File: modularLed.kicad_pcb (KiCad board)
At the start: 2 copper layers, 101.6 x 101.6 mm, 173 parts, among them IC101 ATMEGA328P-A, J101 POWER_JACKPTH, M301 FDS4935BZ, M302 FDS4935BZ, M303 FDS4935BZ, M304 FDS4935BZ, M305 FDS4935BZ, M306 FDS4935BZ, M307 FDS4935BZ, M308 FDS4935BZ, M401 FDS4935BZ, M402 FDS4935BZ, M403 FDS4935BZ, M404 FDS4935BZ, M405 FDS4935BZ, M406 FDS4935BZ, M407 FDS4935BZ, M408 FDS4935BZ, M501 FDS4935BZ, M502 FDS4935BZ, M503 FDS4935BZ, M504 FDS4935BZ, M505 FDS4935BZ, M506 FDS4935BZ, M507 FDS4935BZ, M508 FDS4935BZ, M601 FDS4935BZ, M602 FDS4935BZ, M603 FDS4935BZ, M604 FDS4935BZ, M605 FDS4935BZ, M606 FDS4935BZ, M607 FDS4935BZ, M608 FDS4935BZ, P101 CONN_01X04, P102 CONN_01X04, P103 CONN_01X04, P104 CONN_01X04, P105 CONN_01X06, P106 CONN_01X06, P107 CONN_01X06, P108 CONN_01X06, P109 CONN_02X03, P701 CONN_01X06, U101 ISL83485, U102 R-78E-0.5, U103 TLC5941, U104 74LS283, U105 74LS283, U201 74LS139, U301 74154, U401 74154, U501 74154, U601 74154, U701 ESP-12, U702 ISL83485

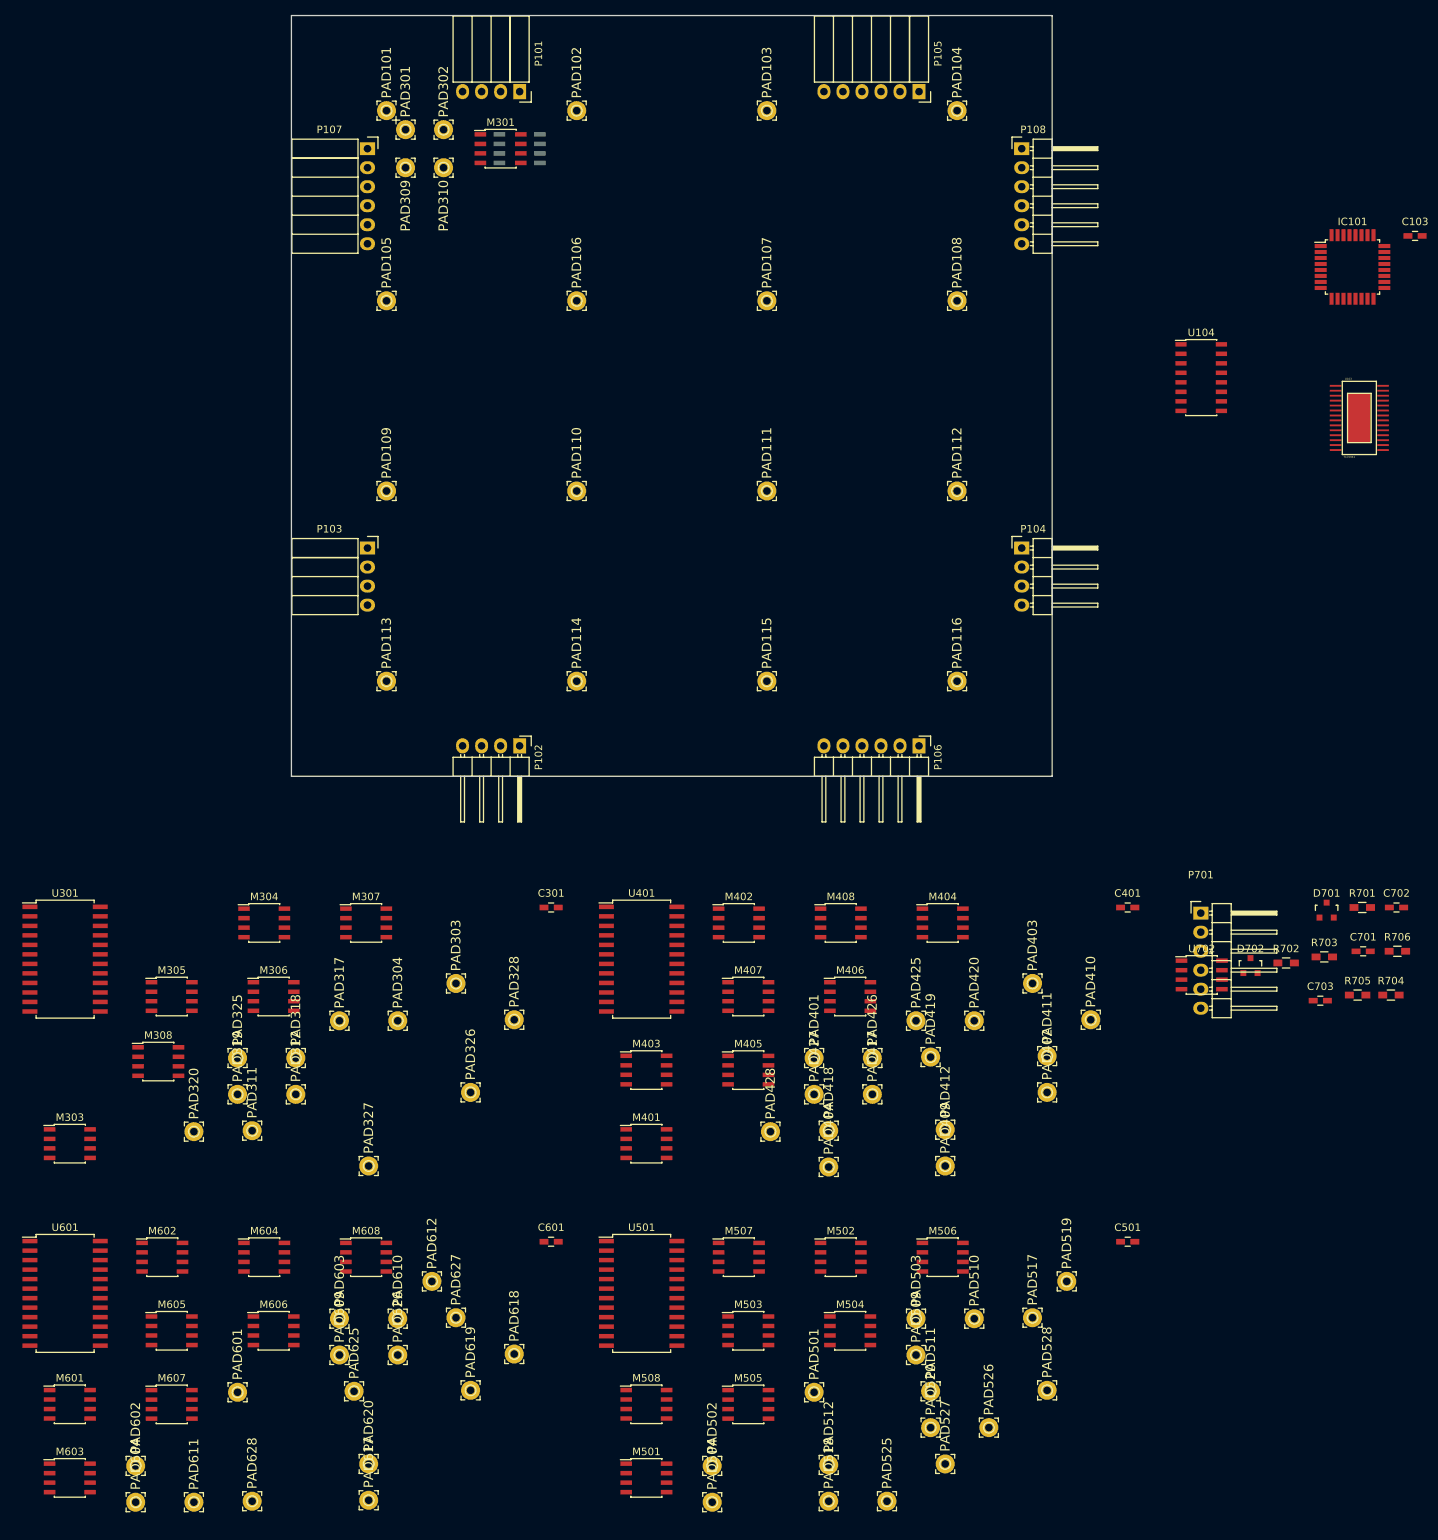
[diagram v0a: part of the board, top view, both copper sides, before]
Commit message: First quadrant of rows
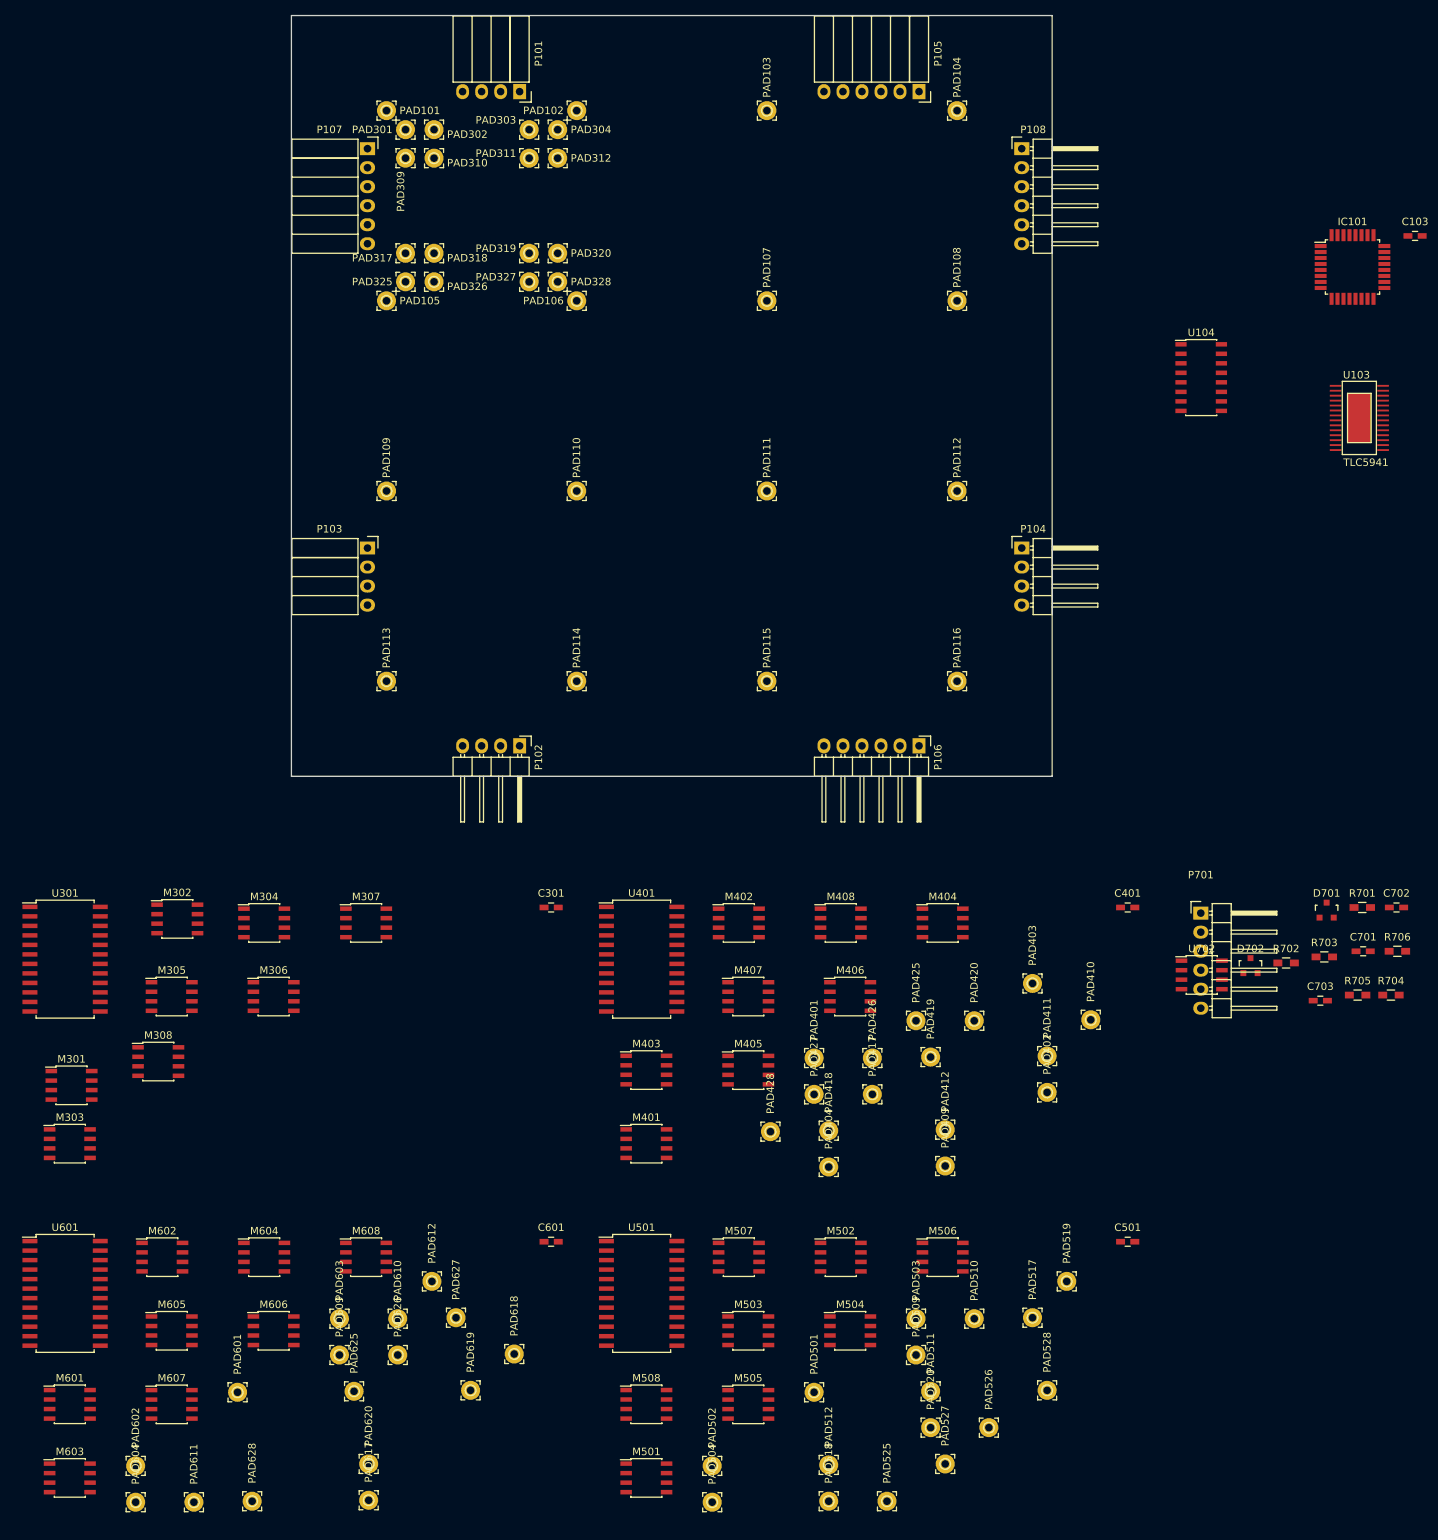
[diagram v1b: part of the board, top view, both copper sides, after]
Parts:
- M302: moved to F.Cu
- moved M301 137.6 mm to (59.5, 193.7)
- moved PAD311 135.0 mm to (120.7, 69.8), turned to 90 degrees
- moved PAD312 129.8 mm to (124.5, 69.8), turned to 270 degrees
- moved PAD320 127.0 mm to (124.5, 82.5), turned to 270 degrees
- moved PAD304 120.9 mm to (124.5, 66.0), turned to 270 degrees
- moved PAD327 120.0 mm to (120.7, 86.4), turned to 90 degrees
- moved PAD319 118.9 mm to (120.7, 82.5), turned to 90 degrees
- moved PAD303 114.4 mm to (120.7, 66.0), turned to 180 degrees
- moved M302 112.6 mm to (73.7, 171.4)
- moved PAD318 109.1 mm to (108.0, 82.5), turned to 270 degrees
- moved PAD326 108.4 mm to (108.0, 86.4), turned to 270 degrees
- moved PAD325 106.1 mm to (104.1, 86.4), turned to 90 degrees
- moved PAD317 102.9 mm to (104.1, 82.5), turned to 90 degrees
- moved PAD328 98.7 mm to (124.5, 86.4), turned to 270 degrees
- moved PAD310 1.80 mm to (108.0, 69.8), turned to 270 degrees
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
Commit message: Second quadrant of rows
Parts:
- moved PAD604 212.3 mm to (175.3, 66.0)
- moved PAD611 203.4 mm to (171.4, 69.8)
- moved PAD602 200.2 mm to (158.8, 66.0)
- moved PAD628 186.9 mm to (175.3, 86.4)
- moved PAD601 183.8 mm to (154.9, 66.0)
- moved PAD620 178.7 mm to (175.3, 82.5)
- moved PAD603 176.1 mm to (171.4, 66.0)
- moved PAD617 175.6 mm to (154.9, 82.5)
- moved PAD609 170.6 mm to (154.9, 69.8)
- moved PAD610 164.7 mm to (158.8, 69.8)
- moved PAD612 164.5 mm to (175.3, 69.8)
- moved PAD619 162.8 mm to (171.4, 82.5)
- moved PAD625 159.0 mm to (154.9, 86.4)
- moved PAD626 153.8 mm to (158.8, 86.4)
- moved PAD618 152.4 mm to (158.8, 82.5)
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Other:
- board text added: "Rows 0-15"
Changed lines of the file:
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@@
     (links 478)
     (no_connects 478)
-    (area 88.824999 50.724999 190.575001 152.475001)
+    (area 28.736999 47.3025 279.520234 278.695311)
     (thickness 1.6)
-    (drawings 4)
+    (drawings 5)
     (tracks 0)
     (zones 0)
@@
   )
   (module Wire_Pads:wirepad-2_54_1_0 (layer F.Cu)
-    (at 81.707143 234.670461)
+    (at 154.94 66.04)
     (descr "THROUGH-HOLE PAD")
     (tags "THROUGH-HOLE PAD")
@@
   )
   (module Wire_Pads:wirepad-2_54_1_0 (layer F.Cu)
-    (at 68.097143 244.500461)
+    (at 158.75 66.04)
     (descr "THROUGH-HOLE PAD")
     (tags "THROUGH-HOLE PAD")
@@
   )
   (module Wire_Pads:wirepad-2_54_1_0 (layer F.Cu)
-    (at 95.317143 224.840461)
+    (at 171.45 66.04)
     (descr "THROUGH-HOLE PAD")
     (tags "THROUGH-HOLE PAD")
@@
   )
   (module Wire_Pads:wirepad-2_54_1_0 (layer F.Cu)
-    (at 68.097143 249.350461)
+    (at 175.26 66.04)
     (descr "THROUGH-HOLE PAD")
     (tags "THROUGH-HOLE PAD")
@@
   )
   (module Wire_Pads:wirepad-2_54_1_0 (layer F.Cu)
-    (at 95.317143 229.690461)
+    (at 154.94 69.85)
     (descr "THROUGH-HOLE PAD")
     (tags "THROUGH-HOLE PAD")
@@
   )
   (module Wire_Pads:wirepad-2_54_1_0 (layer F.Cu)
-    (at 103.097143 224.840461)
+    (at 158.75 69.85)
     (descr "THROUGH-HOLE PAD")
     (tags "THROUGH-HOLE PAD")
@@
   )
   (module Wire_Pads:wirepad-2_54_1_0 (layer F.Cu)
-    (at 75.877143 249.350461)
+    (at 171.45 69.85)
     (descr "THROUGH-HOLE PAD")
     (tags "THROUGH-HOLE PAD")
@@
   )
   (module Wire_Pads:wirepad-2_54_1_0 (layer F.Cu)
-    (at 107.667143 219.860461)
+    (at 175.26 69.85)
     (descr "THROUGH-HOLE PAD")
     (tags "THROUGH-HOLE PAD")
@@
   )
   (module Wire_Pads:wirepad-2_54_1_0 (layer F.Cu)
-    (at 83.657143 249.220461)
+    (at 175.26 86.36)
     (descr "THROUGH-HOLE PAD")
     (tags "THROUGH-HOLE PAD")
@@
   )
   (module Wire_Pads:wirepad-2_54_1_0 (layer F.Cu)
-    (at 110.877143 224.710461)
+    (at 171.45 86.36)
     (descr "THROUGH-HOLE PAD")
     (tags "THROUGH-HOLE PAD")
@@
   )
   (module Wire_Pads:wirepad-2_54_1_0 (layer F.Cu)
-    (at 103.097143 229.690461)
+    (at 158.75 86.36)
     (descr "THROUGH-HOLE PAD")
     (tags "THROUGH-HOLE PAD")
@@
   )
   (module Wire_Pads:wirepad-2_54_1_0 (layer F.Cu)
-    (at 97.267143 234.540461)
+    (at 154.94 86.36)
     (descr "THROUGH-HOLE PAD")
     (tags "THROUGH-HOLE PAD")
@@
   )
   (module Wire_Pads:wirepad-2_54_1_0 (layer F.Cu)
-    (at 99.217143 244.240461)
+    (at 175.26 82.55)
     (descr "THROUGH-HOLE PAD")
     (tags "THROUGH-HOLE PAD")
@@
   )
   (module Wire_Pads:wirepad-2_54_1_0 (layer F.Cu)
-    (at 112.827143 234.410461)
+    (at 171.45 82.55)
     (descr "THROUGH-HOLE PAD")
     (tags "THROUGH-HOLE PAD")
@@
   )
   (module Wire_Pads:wirepad-2_54_1_0 (layer F.Cu)
-    (at 118.657143 229.560461)
+    (at 158.75 82.55)
     (descr "THROUGH-HOLE PAD")
     (tags "THROUGH-HOLE PAD")
@@
   )
   (module Wire_Pads:wirepad-2_54_1_0 (layer F.Cu)
-    (at 99.217143 249.090461)
+    (at 154.94 82.55)
     (descr "THROUGH-HOLE PAD")
     (tags "THROUGH-HOLE PAD")
@@
       (net 206 "Net-(PAD109-Pad1)"))
   )
+  (gr_text "Rows 0-15" (at 114.3 88.9) (layer F.SilkS)
+    (effects (font (size 1 1) (thickness 0.15)))
+  )
   (gr_line (start 88.9 152.4) (end 88.9 50.8) (layer Edge.Cuts) (width 0.15))

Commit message: Third quadrant of rows
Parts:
- moved PAD402 112.9 mm to (108.0, 116.8), turned to 270 degrees
- moved PAD409 110.5 mm to (104.1, 120.7), turned to 90 degrees
- moved PAD410 108.7 mm to (108.0, 120.7), turned to 270 degrees
- moved PAD411 97.8 mm to (120.7, 120.7), turned to 90 degrees
- moved PAD404 94.9 mm to (124.5, 116.8), turned to 270 degrees
- moved PAD412 94.4 mm to (124.5, 120.7), turned to 270 degrees
- moved PAD403 92.3 mm to (120.7, 116.8), turned to 90 degrees
- moved PAD401 91.3 mm to (104.1, 116.8), turned to 90 degrees
- moved PAD417 87.6 mm to (104.1, 133.3), turned to 90 degrees
- moved PAD418 84.8 mm to (108.0, 133.3), turned to 270 degrees
- moved PAD425 83.3 mm to (104.1, 137.2), turned to 90 degrees
- moved PAD426 78.9 mm to (108.0, 137.2), turned to 270 degrees
- moved PAD419 77.9 mm to (120.7, 133.3), turned to 90 degrees
- moved PAD420 76.0 mm to (124.5, 133.3), turned to 270 degrees
- moved PAD427 69.1 mm to (120.7, 137.2), turned to 90 degrees
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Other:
- board text added: "Rows 16-31"
- board text added: "Rows 32-47"

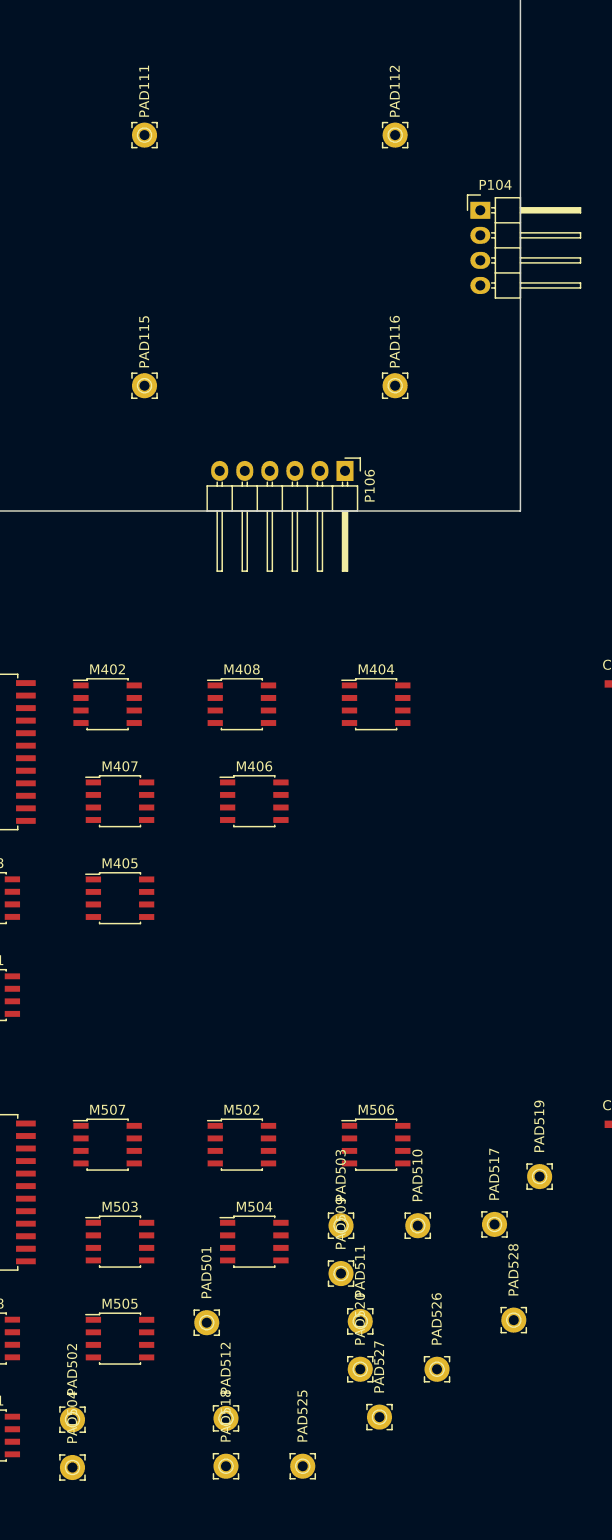
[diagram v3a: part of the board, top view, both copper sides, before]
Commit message: Fourth quadrant of rows
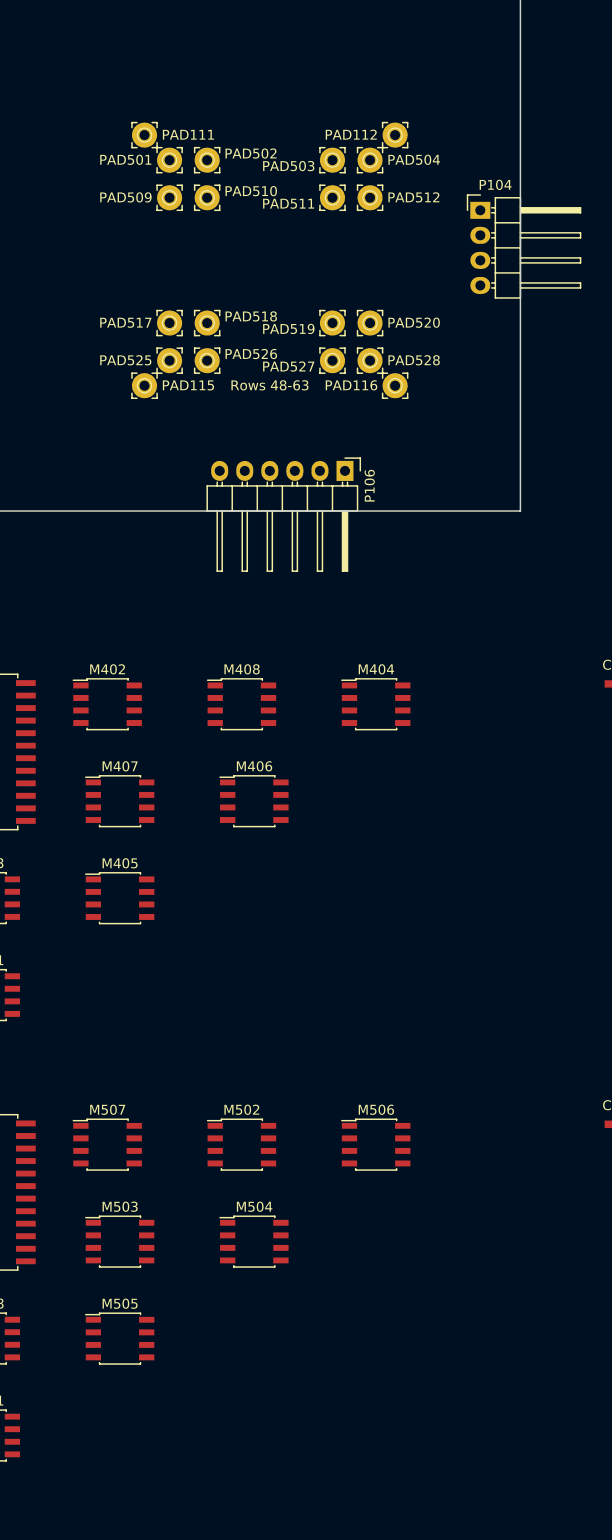
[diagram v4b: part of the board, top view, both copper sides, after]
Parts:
- moved PAD504 135.9 mm to (175.3, 116.8), turned to 270 degrees
- moved PAD502 128.4 mm to (158.8, 116.8), turned to 270 degrees
- moved PAD512 124.6 mm to (175.3, 120.7), turned to 270 degrees
- moved PAD501 117.9 mm to (154.9, 116.8), turned to 90 degrees
- moved PAD518 115.9 mm to (158.8, 133.3), turned to 270 degrees
- moved PAD511 113.9 mm to (171.4, 120.7), turned to 90 degrees
- moved PAD525 112.9 mm to (154.9, 137.2), turned to 90 degrees
- moved PAD509 110.4 mm to (154.9, 120.7), turned to 90 degrees
- moved PAD503 108.0 mm to (171.4, 116.8), turned to 90 degrees
- moved PAD527 107.2 mm to (171.4, 137.2), turned to 90 degrees
- moved PAD510 106.4 mm to (158.8, 120.7), turned to 270 degrees
- moved PAD520 106.0 mm to (175.3, 133.3), turned to 270 degrees
- moved PAD526 104.9 mm to (158.8, 137.2), turned to 270 degrees
- moved PAD528 98.3 mm to (175.3, 137.2), turned to 270 degrees
- moved PAD517 97.1 mm to (154.9, 133.3), turned to 90 degrees
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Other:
- board text added: "Rows 48-63"

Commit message: First quadrant of fets placed
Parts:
- M303, M305, M307, M308: moved to B.Cu
- moved M303 144.4 mm to (114.3, 67.9)
- moved M301 141.4 mm to (106.7, 60.3), turned to 270 degrees
- moved M308 125.9 mm to (123.8, 76.2), turned to 270 degrees
- moved M305 110.5 mm to (105.4, 76.2), turned to 270 degrees
- moved M302 108.8 mm to (114.3, 70.5), turned to 180 degrees
- moved U301 106.4 mm to (38.1, 72.4)
- moved M306 103.7 mm to (114.3, 81.9), turned to 180 degrees
- moved M304 103.3 mm to (123.8, 76.2), turned to 90 degrees
- moved M307 88.9 mm to (114.3, 84.5)
- turned PAD101 to 90 degrees
- turned PAD105 to 90 degrees
- turned PAD310 to 180 degrees
- turned PAD311 to 180 degrees
- turned PAD318 to 0 degrees
- turned PAD319 to 0 degrees

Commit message: Second and third quadrant of fets placed
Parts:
- M403, M405, M407, M408, M603, M605, M607, M608, U401, U701: moved to B.Cu
- moved J101 218.2 mm to (85.0, 55.9), turned to 270 degrees
- moved M603 207.2 mm to (165.1, 67.9)
- moved P109 197.5 mm to (58.4, 73.7)
- moved M601 187.8 mm to (157.5, 76.2), turned to 90 degrees
- moved U101 182.6 mm to (152.4, 101.6)
- moved M607 177.5 mm to (164.9, 84.5)
- moved M602 171.9 mm to (165.1, 72.4), turned to 180 degrees
- moved M605 171.8 mm to (156.2, 76.2), turned to 270 degrees
- moved M604 166.4 mm to (174.6, 76.2), turned to 90 degrees
- moved M606 166.1 mm to (164.9, 80.0), turned to 180 degrees
- moved M608 159.0 mm to (173.4, 76.2), turned to 270 degrees
- moved P701 139.1 mm to (133.3, 54.9), turned to 90 degrees
- moved U102 132.2 mm to (126.4, 101.6), turned to 270 degrees
- moved U201 124.7 mm to (74.9, 141.0)
- moved U701 104.3 mm to (132.1, 81.3)
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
